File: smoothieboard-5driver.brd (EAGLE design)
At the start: 129.5 x 105.1 mm, 253 parts, among them IC1 LPC1769, IC10 LM1117-3.3V, IC11 78L12F, IC12 A4982, IC2 A4982, IC3 A4982, IC4 MCP44X1, IC5 A4982, IC6 A4982, IC9 MCP44X1, J10 POWER_JACKSMD, Q1 BSL207SP, Q2 12MHz, Q3 25MHz, Q6 AOT240L, Q7 AOT240L, Q8 ZXMN4A06GTA, Q9 ZXMN4A06GTA, U1 USD-SOCKETNEW, X14 USBPTH

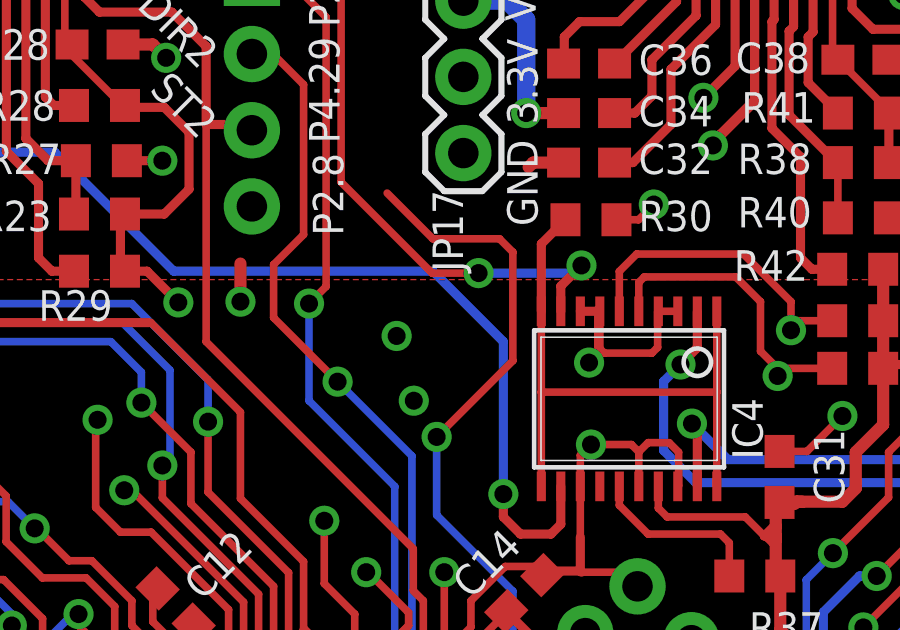
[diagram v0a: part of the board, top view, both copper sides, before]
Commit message: ditch vestige of STP5 signal's previous incarnation
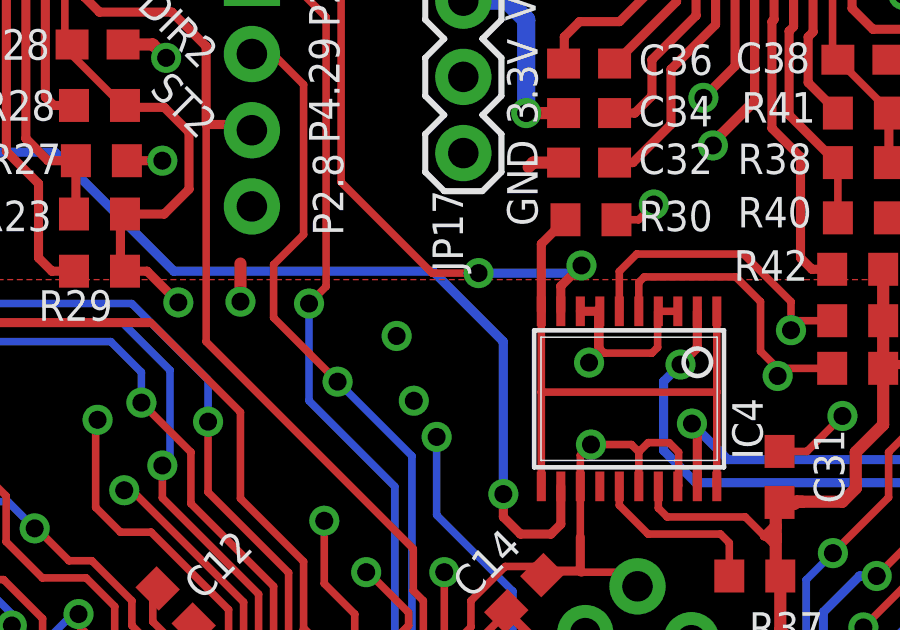
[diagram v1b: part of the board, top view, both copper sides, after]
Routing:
- net STP5: track 114.0 -> 101.7 mm
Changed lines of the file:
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@@
 <layer number="14" name="Route14" color="1" fill="6" visible="no" active="no"/>
 <layer number="15" name="Route15" color="5" fill="1" visible="no" active="yes"/>
-<layer number="16" name="Bottom" color="1" fill="1" visible="no" active="yes"/>
+<layer number="16" name="Bottom" color="1" fill="1" visible="yes" active="yes"/>
 <layer number="17" name="Pads" color="2" fill="1" visible="yes" active="yes"/>
 <layer number="18" name="Vias" color="2" fill="1" visible="yes" active="yes"/>
@@
 <wire x1="58.293" y1="51.3252125" x2="58.293" y2="52.5145" width="0.254" layer="1"/>
 <wire x1="58.293" y1="52.5145" x2="57.9755" y2="52.832" width="0.254" layer="1"/>
-<wire x1="53.7845" y1="69.0245" x2="55.3085" y2="67.5005" width="0.254" layer="1"/>
-<wire x1="55.3085" y1="67.5005" x2="57.531" y2="67.5005" width="0.254" layer="1"/>
-<wire x1="57.531" y1="67.5005" x2="57.9755" y2="67.056" width="0.254" layer="1"/>
-<wire x1="57.9755" y1="67.056" x2="57.9755" y2="63.4365" width="0.254" layer="1"/>
-<wire x1="57.9755" y1="63.4365" x2="55.4355" y2="60.8965" width="0.254" layer="1"/>
 <via x="55.4355" y="60.8965" extent="1-16" drill="0.6"/>
 <wire x1="55.4355" y1="60.8965" x2="55.4355" y2="58.293" width="0.254" layer="16"/>

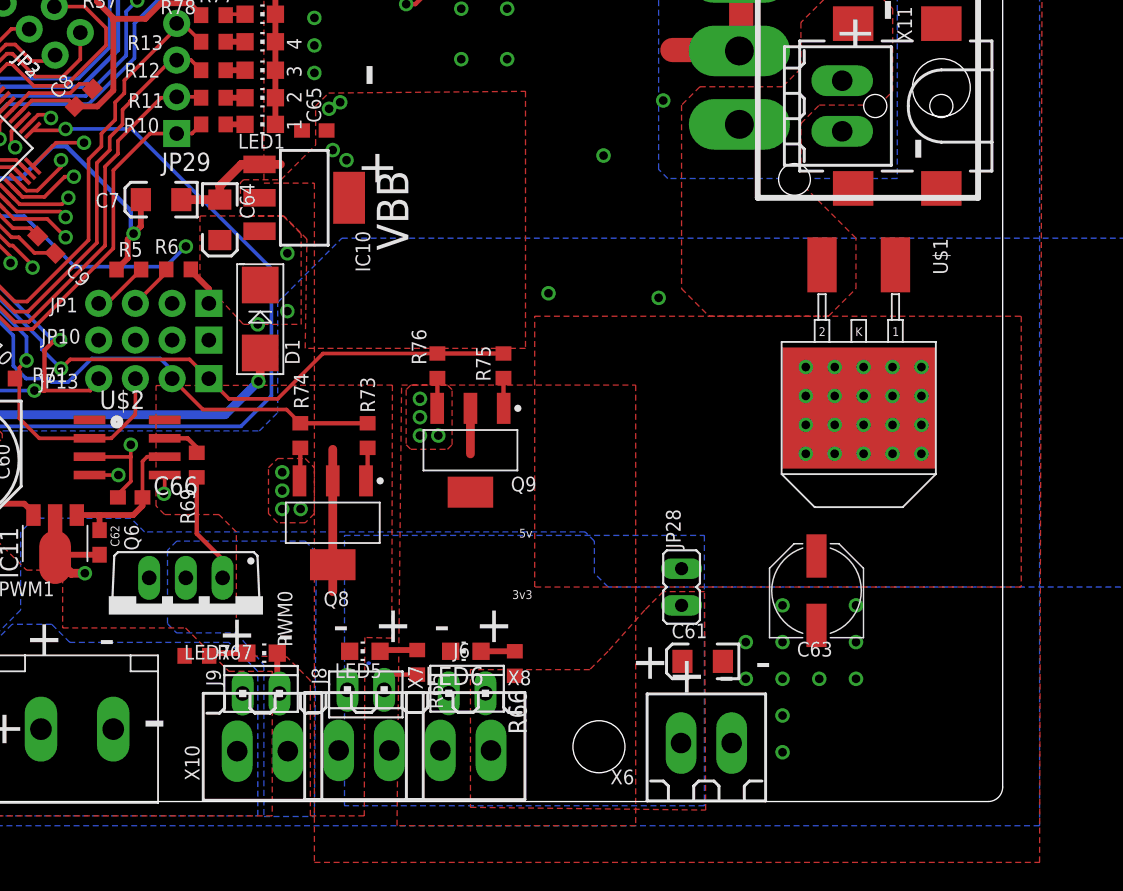
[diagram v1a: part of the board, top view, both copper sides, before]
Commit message: Initial placement of extra mosfets
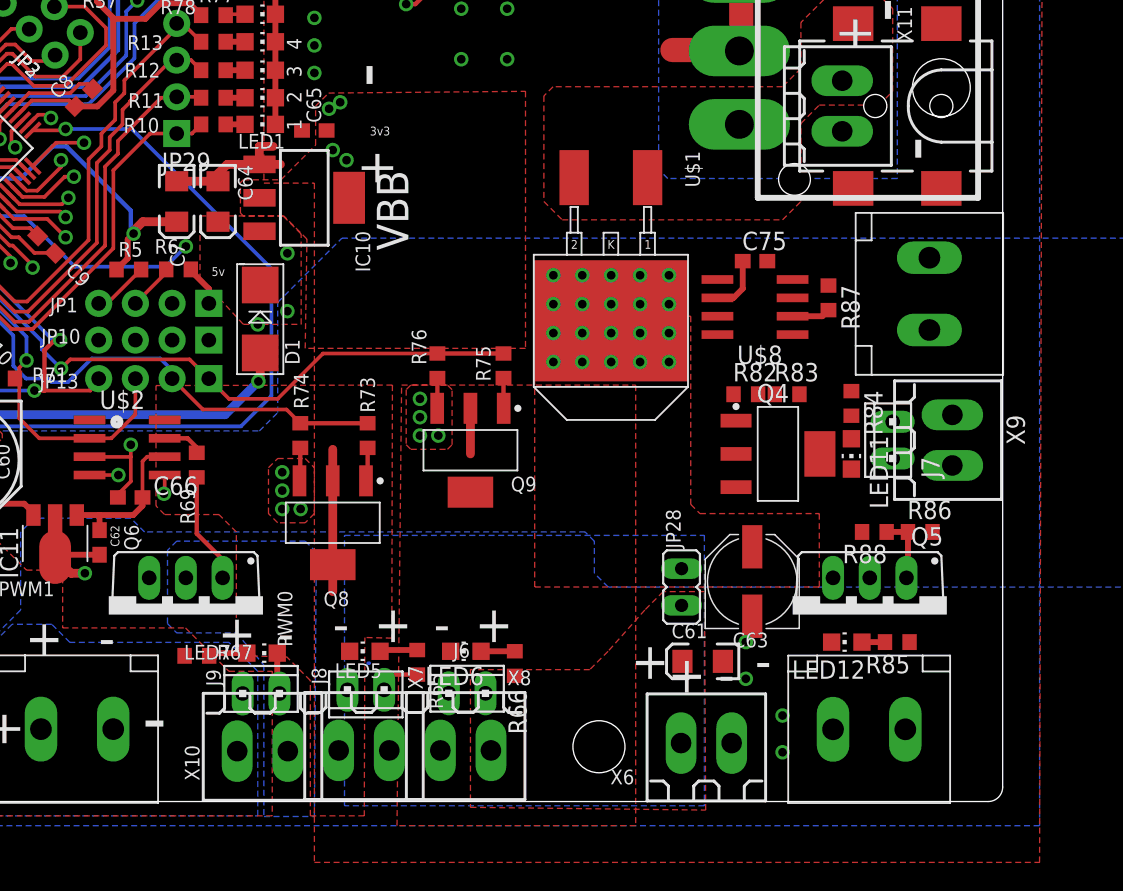
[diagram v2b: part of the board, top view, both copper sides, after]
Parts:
- added C75: .1uF, resistor:C0603
- added J7: (no value), con-amp:10X02MTA
- added LED11, LED12: (no value), led:CHIP-LED0805
- added Q4: ZXMN4A06, ipc-7351-transistor:SOT230P700X160-4N
- added Q5: AOT240L, transistor-power:TO220BV
- added R82, R88: 22R, resistor:R0603
- added R83, R86, R87: 10k, resistor:R0603
- added R84, R85: 5.6K, resistor:R0603
- added U$7, U$9: 5MMCONN, eric_sorensen:1715250000
- added U$8: TC4427, custom_esorensen:SOIC8
- added X9: (no value), con-weidmueller-sl35:180G-2
- Q8, Q9: value ZXMN4A06GTA -> ZXMN4A06
- moved U$1 18.2 mm to (108.8, 44.8)
- moved C63 4.49 mm to (112.2, 14.4)
- moved C64 1.28 mm to (75.2, 40.6)
- moved C7 1.09 mm to (72.4, 40.6), turned to 270 degrees
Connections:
- new net GPIO_FET1: Q5.G, R86.1, R88.1
- new net MOSFET_DRIVE1: J7.1, R84.1, R85.1, U$7.P$2, U$9.P$2, X9.1
- new net N$100: LED11.A, R84.2
- new net N$109: LED12.C, Q5.D, U$7.P$1
- new net N$110: LED12.A, R85.2
- new net N$113: R88.2, U$8.7
- new net N$52: J7.2, LED11.C, Q4.4, X9.2
- new net N$97: Q4.1, R82.1
- net 12VREG: now also C75.1, U$8.6
- net GND: now also C75.2, Q4.3, Q5.S, R83.2, R86.2, R87.1, U$8.3, U$9.P$1
- net P1_22: now also R82.2, R83.1
- net P1_23: now also R87.2, U$8.2
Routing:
- net GPIO_FET1: track 0.00 -> 4.69 mm
- net 12VREG: track 10.6 -> 14.5 mm
- net P1_23: track 28.4 -> 31.1 mm
- net GND: track 266.8 -> 268.6 mm, vias 338 -> 327
- net N$110: track 0.00 -> 1.59 mm
- net 3.3V: track 300.4 -> 301.3 mm

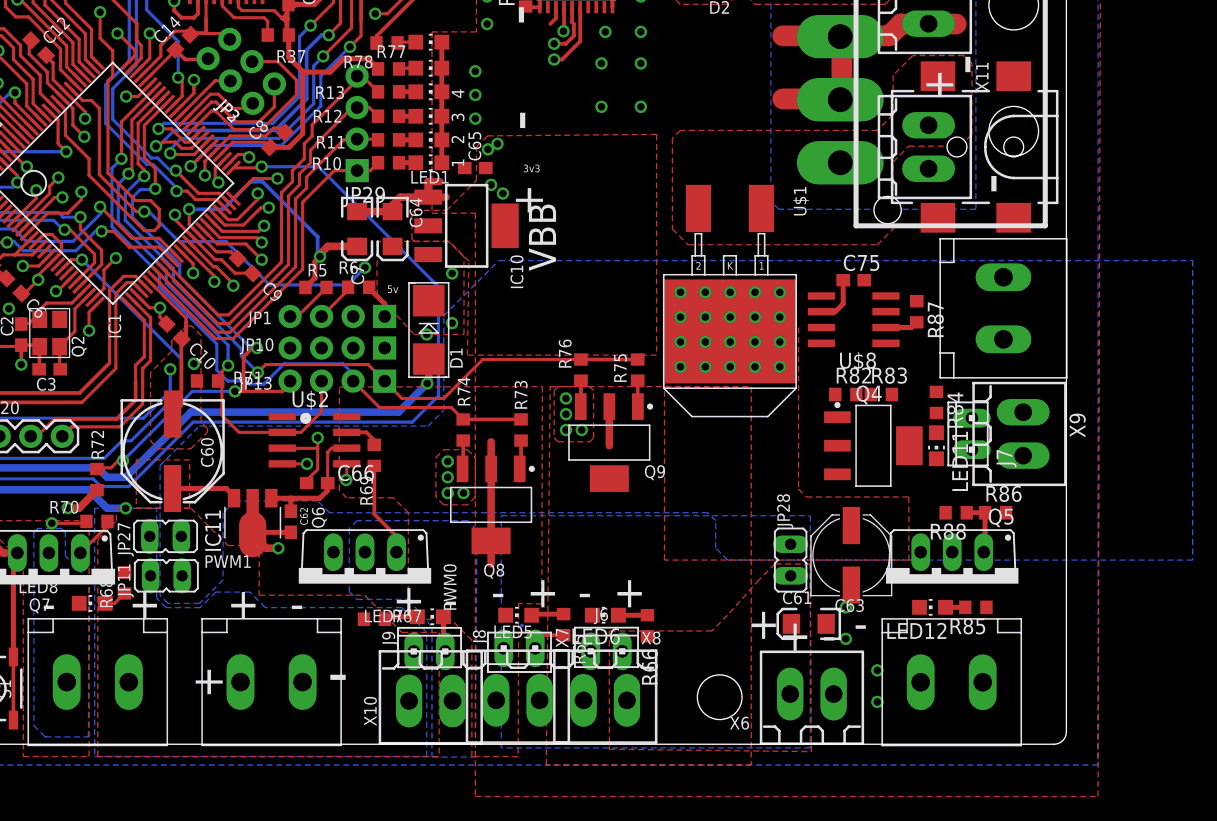
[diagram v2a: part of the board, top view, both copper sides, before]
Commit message: Extra mosfets routed
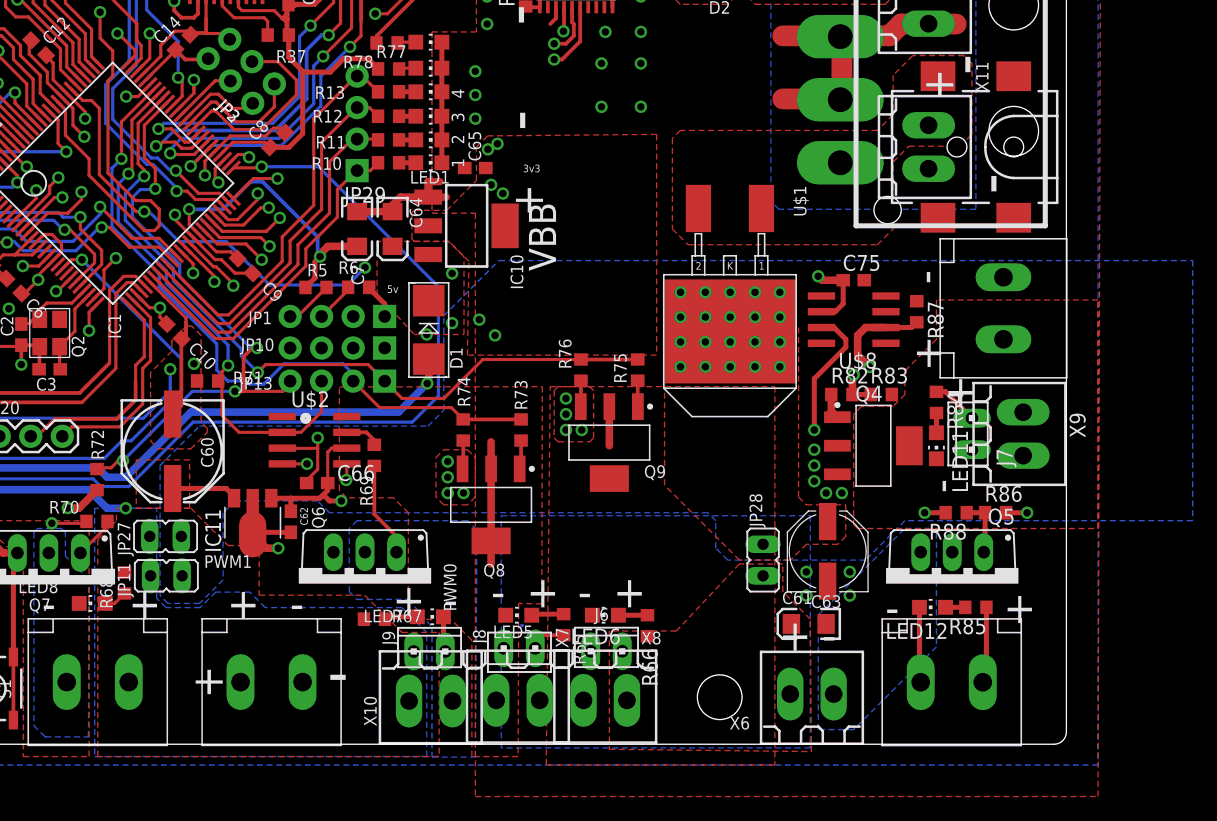
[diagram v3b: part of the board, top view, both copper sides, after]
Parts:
- moved JP28 2.22 mm to (105.1, 14.0)
- moved C63 1.93 mm to (110.3, 14.7)
- moved R82 0.32 mm to (111.4, 27.3)
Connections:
- net GND: now also U$9.P$2; no longer U$9.P$1
- net MOSFET_DRIVE1: now also U$9.P$1; no longer U$9.P$2
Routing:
- net P1_23: track 31.1 -> 118.3 mm, vias 2 -> 4
- net P1_22: track 22.5 -> 107.0 mm, vias 2 -> 4
- net 12VREG: track 14.5 -> 71.7 mm, vias 0 -> 2
- net N$113: track 0.00 -> 24.1 mm, vias 0 -> 2
- net GND: track 268.6 -> 281.1 mm, vias 327 -> 333
- net MOSFET_DRIVE1: track 0.00 -> 9.89 mm
- net N$109: track 0.00 -> 6.21 mm
- net ISP_BOOT: track 48.7 -> 51.2 mm
- net Z_MAX: track 63.6 -> 65.8 mm
- net N$97: track 0.00 -> 2.03 mm
- net N$100: track 0.00 -> 1.59 mm
- net LED1: track 29.1 -> 28.0 mm
- net SD_CD: track 38.7 -> 38.1 mm
- added copper zone on layer 2, net MOSFET_DRIVE1
- added copper zone on layer 15, net N$109
- added copper zone on layer 1, net N$52

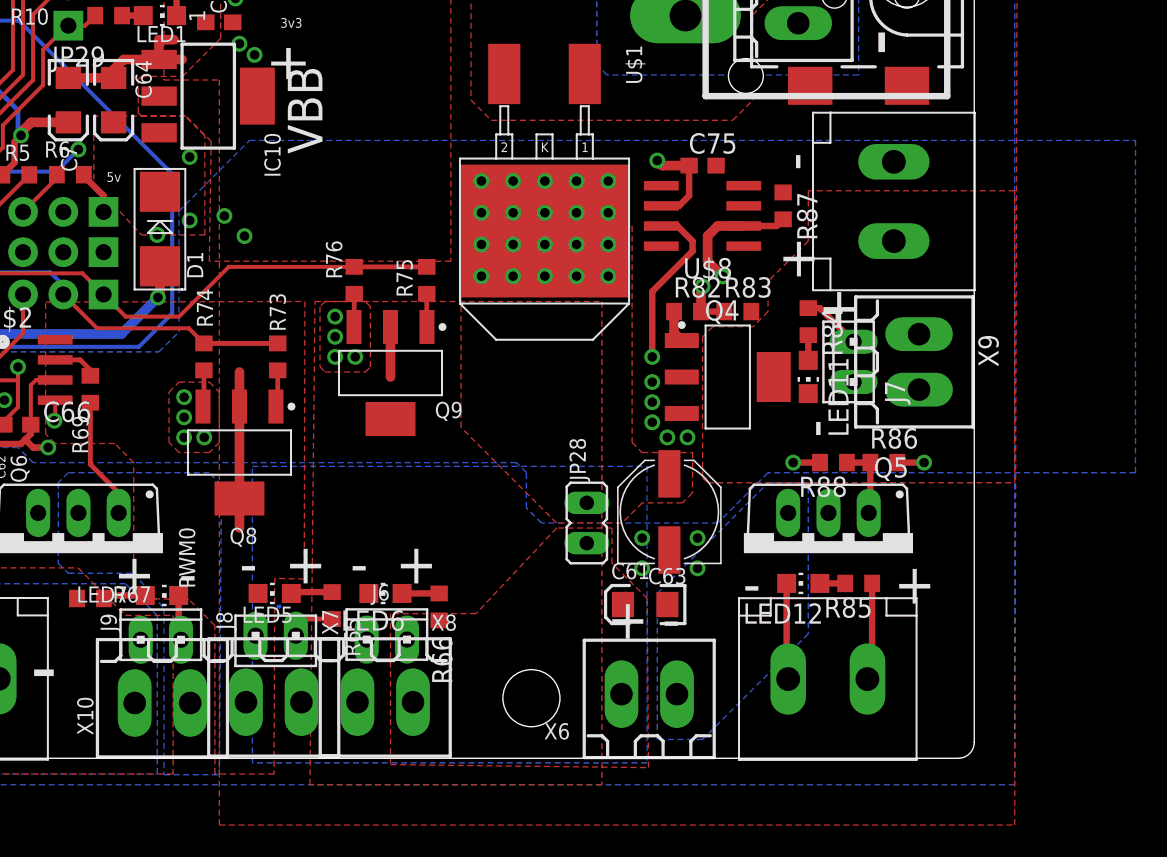
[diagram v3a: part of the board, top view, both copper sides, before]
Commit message: use thermal vias to improve heatsinking for Q4 (small mosfet #3)
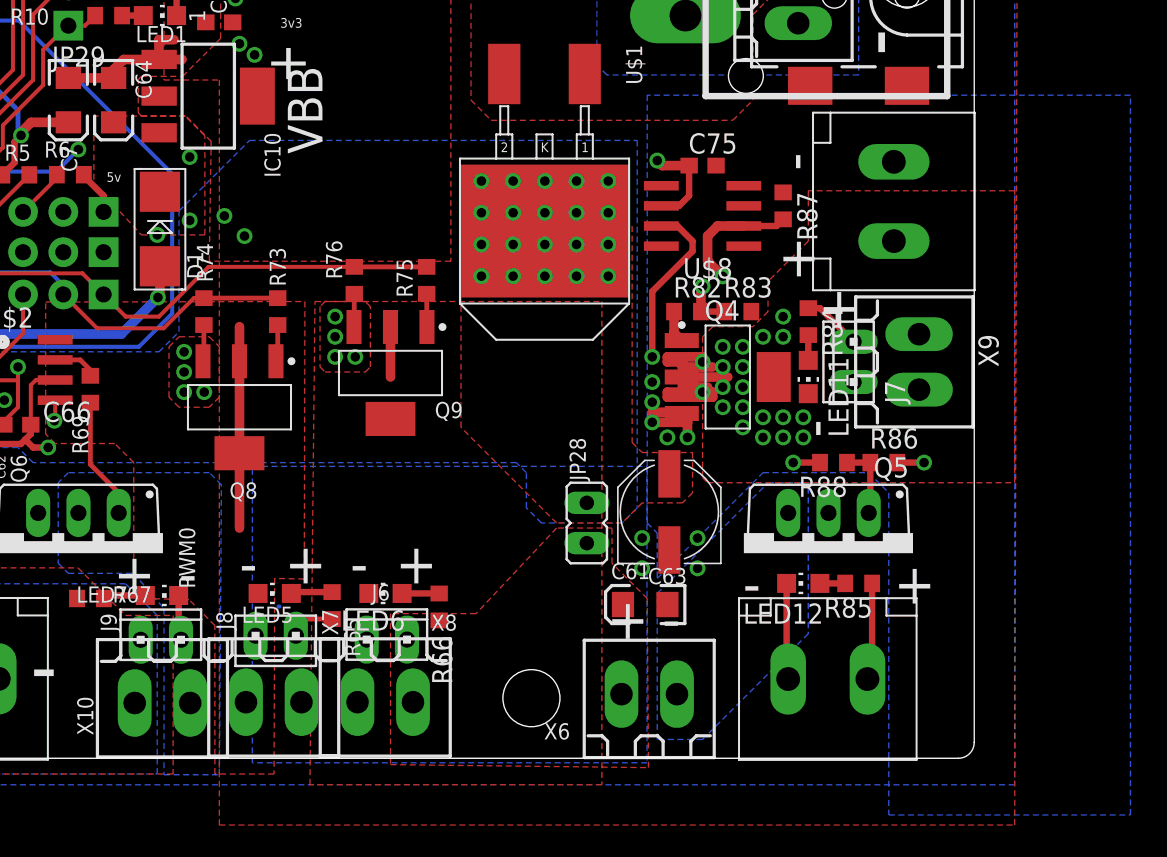
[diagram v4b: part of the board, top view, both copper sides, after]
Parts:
- moved Q8 2.86 mm to (83.2, 21.3)
- moved R73 2.86 mm to (85.6, 27.3)
- moved R74 2.86 mm to (80.9, 27.3)
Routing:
- net N$52: track 0.00 -> 19.1 mm, vias 0 -> 20
- net GND: track 281.1 -> 287.8 mm
- net N$88: track 9.84 -> 12.7 mm
- added copper zone on layer 16, net N$52

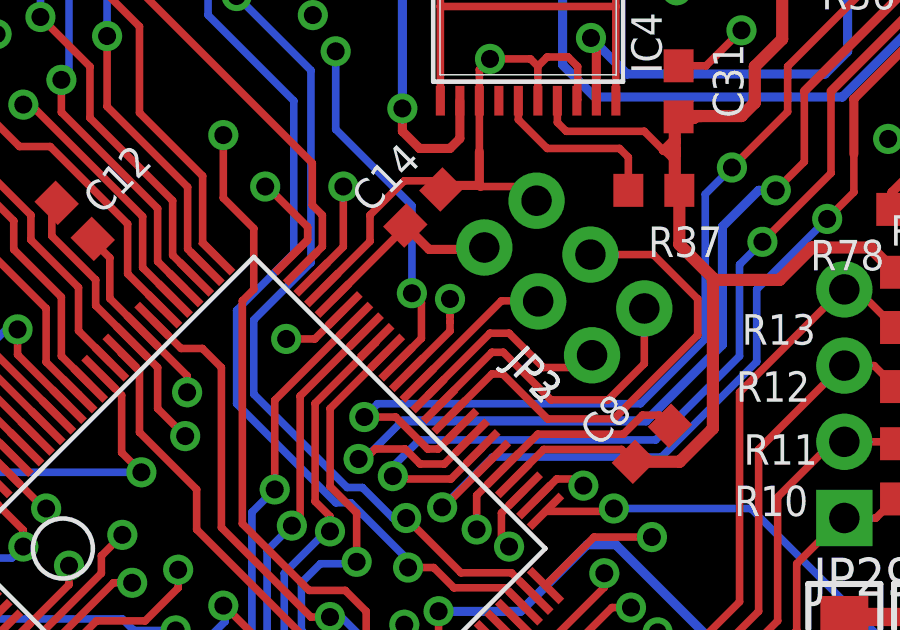
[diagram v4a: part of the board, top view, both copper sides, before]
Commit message: Improve ground plane beneath uC by moving a bunch of traces around
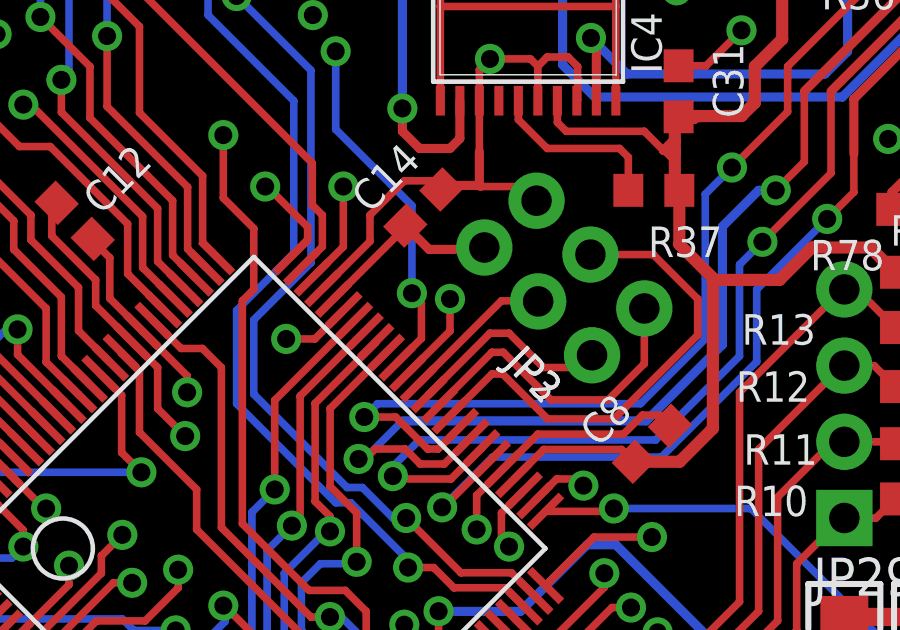
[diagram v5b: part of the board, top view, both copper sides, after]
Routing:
- net SD_CD: track 38.1 -> 35.1 mm
- net ISP_BOOT: track 51.2 -> 48.6 mm
- net PLAY_LED: track 120.1 -> 119.5 mm
